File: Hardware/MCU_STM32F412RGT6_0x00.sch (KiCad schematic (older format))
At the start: 77 parts, among them J1 USB_B_Mini, J2 Conn_01x04, J3 Conn_01x04, J4 Conn_01x04, J5 Conn_01x03, J6 Conn_01x04, U1 STM32F412RGTx, U2 NUP4202, U3 MS5611-01BA, Y1 Crystal_GND24_Small

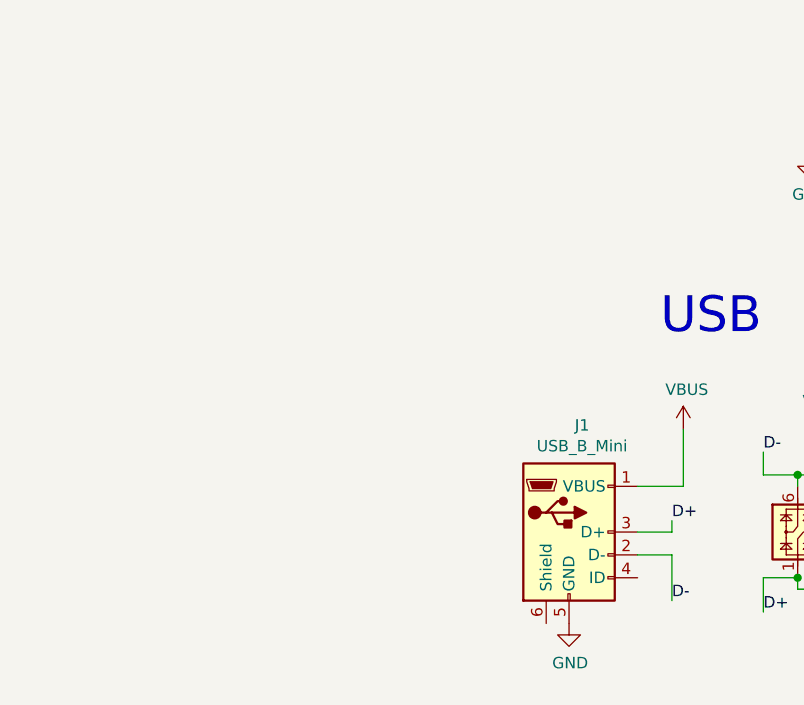
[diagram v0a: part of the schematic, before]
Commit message: new usb connector and pcb size defined
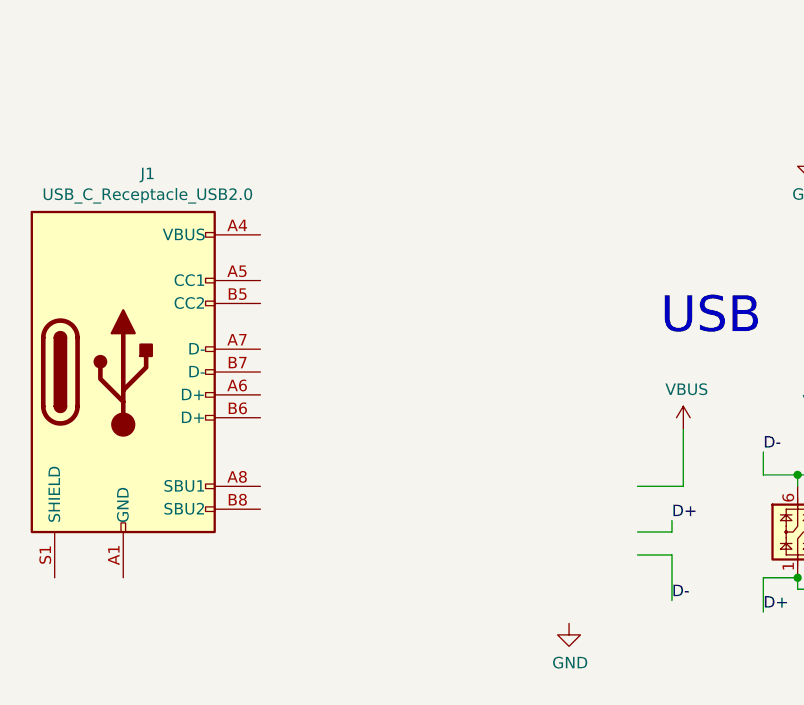
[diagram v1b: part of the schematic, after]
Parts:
- removed J1: USB_B_Mini, Connector_USB:USB_Mini-B_Lumberg_2486_01_Horizontal, symbol Connector:USB_B_Mini
- added J1: USB_C_Receptacle_USB2.0, Connector_USB:USB_C_Receptacle_GCT_USB4085, symbol Connector:USB_C_Receptacle_USB2.0
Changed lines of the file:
@@
 	6050 7050 6050 6950
-$Comp
-L Connector:USB_B_Mini J1
-U 1 1 626CA4B7
-P 850 7050
-F 0 "J1" H 907 7517 50  0000 C CNN
-F 1 "USB_B_Mini" H 907 7426 50  0000 C CNN
-F 2 "Connector_USB:USB_Mini-B_Lumberg_2486_01_Horizontal" H 1000 7000 50  0001 C CNN
-F 3 "~" H 1000 7000 50  0001 C CNN
-	1    850  7050
-	1    0    0    -1
-$EndComp
 $Comp
 L power:GND #PWR0117
@@
 	1    0    0    -1
 $EndComp
+$Comp
+L Connector:USB_C_Receptacle_USB2.0 J1
+U 1 1 62E0D195
+P -1100 6350
+F 0 "J1" H -993 7217 50  0000 C CNN
+F 1 "USB_C_Receptacle_USB2.0" H -993 7126 50  0000 C CNN
+F 2 "Connector_USB:USB_C_Receptacle_GCT_USB4085" H -950 6350 50  0001 C CNN
+F 3 "https://www.usb.org/sites/default/files/documents/usb_type-c.zip" H -950 6350 50  0001 C CNN
+	1    -1100 6350
+	1    0    0    -1
+$EndComp
